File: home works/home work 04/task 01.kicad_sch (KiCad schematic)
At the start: 4 parts, among them Q2 BC328, SW1 SW_Push

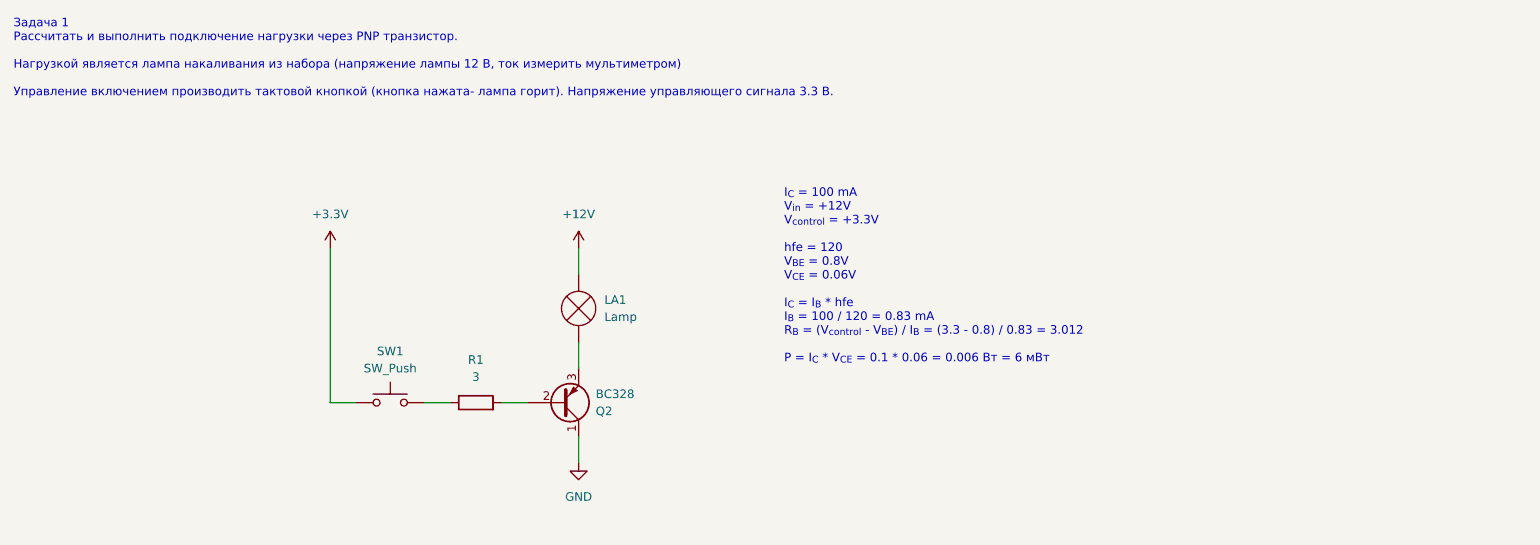
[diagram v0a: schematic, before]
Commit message: fix schema for hw 4.1
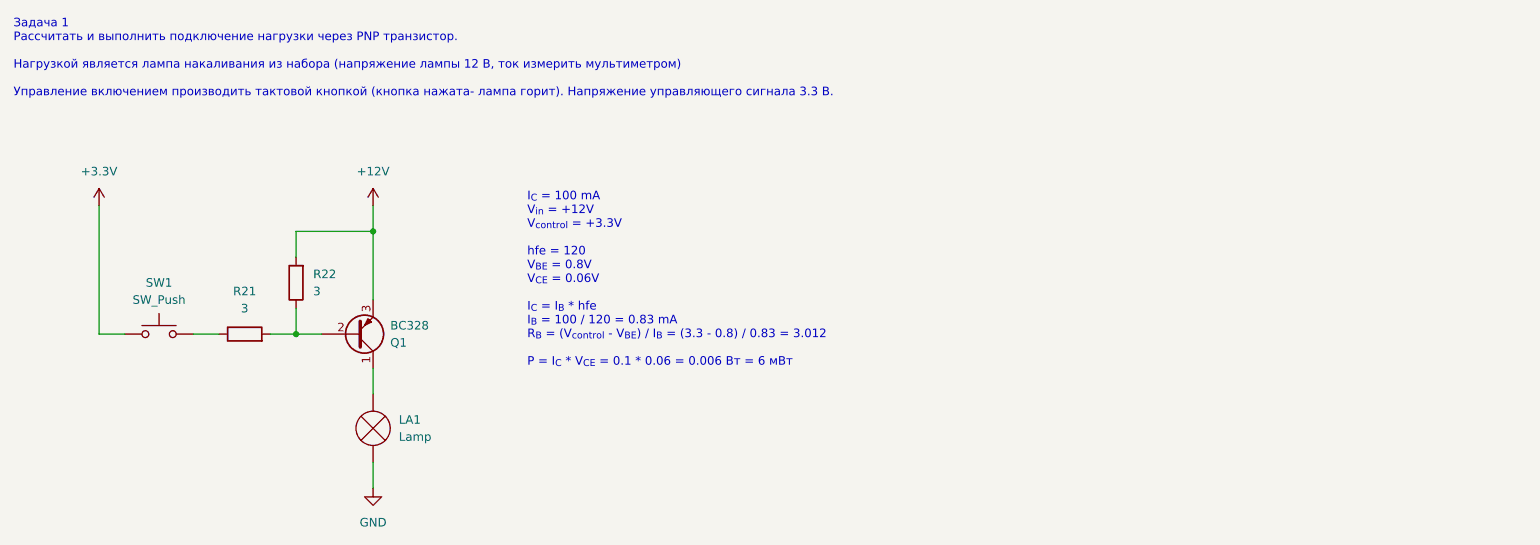
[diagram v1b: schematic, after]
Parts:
- added R22: 3, symbol Device:R
- renumbered Q2 to Q1, R1 to R21
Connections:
- net +12V: now also Q1.3 (E), R22.2; no longer LA1.2 (+)
- net GND: now also LA1.1 (-); no longer Q1.1 (C)
- net at Q1.2 (B), R21.2: now also R22.1
- new net: LA1.2 (+), Q1.1 (C)
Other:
- moved on the sheet: LA1, Q1, R21, SW1
